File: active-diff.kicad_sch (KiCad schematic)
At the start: 13 parts, among them J1 INPUT+

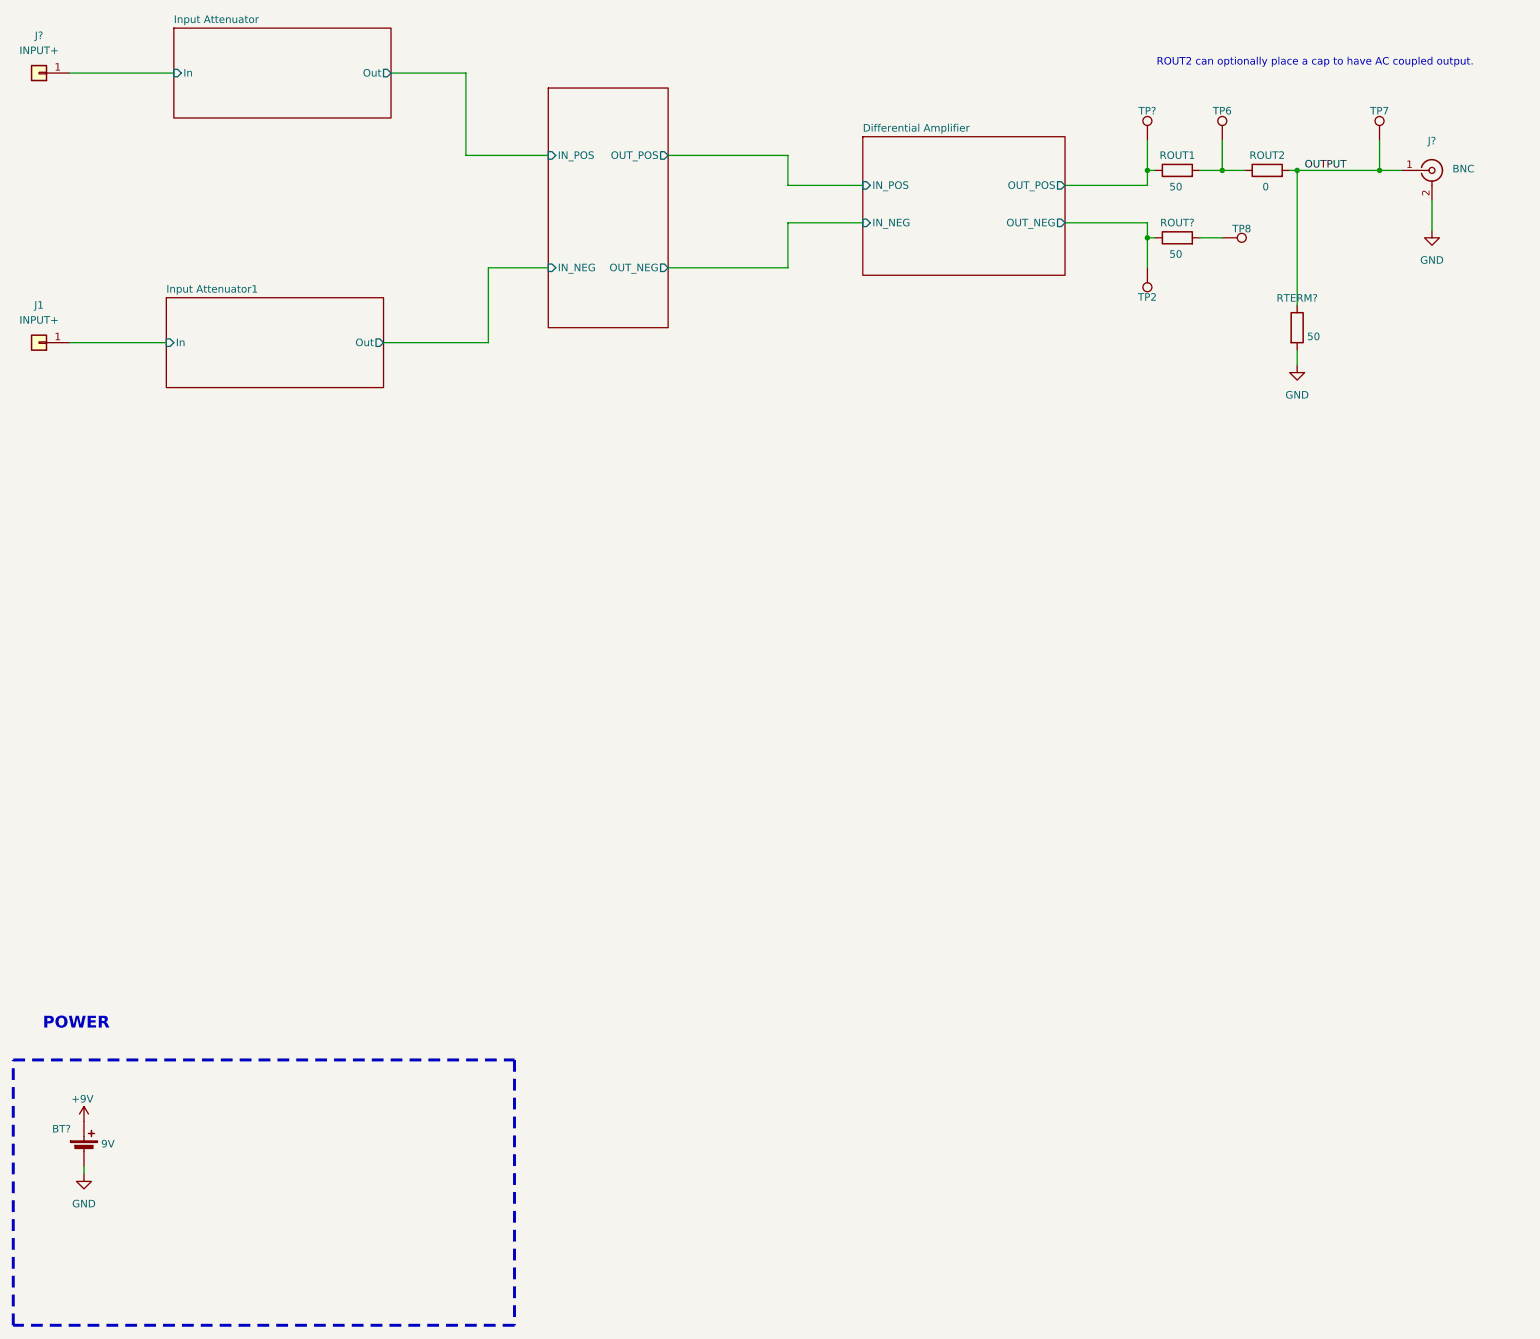
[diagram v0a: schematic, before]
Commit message: DRC completed. Need to add some 3D models.
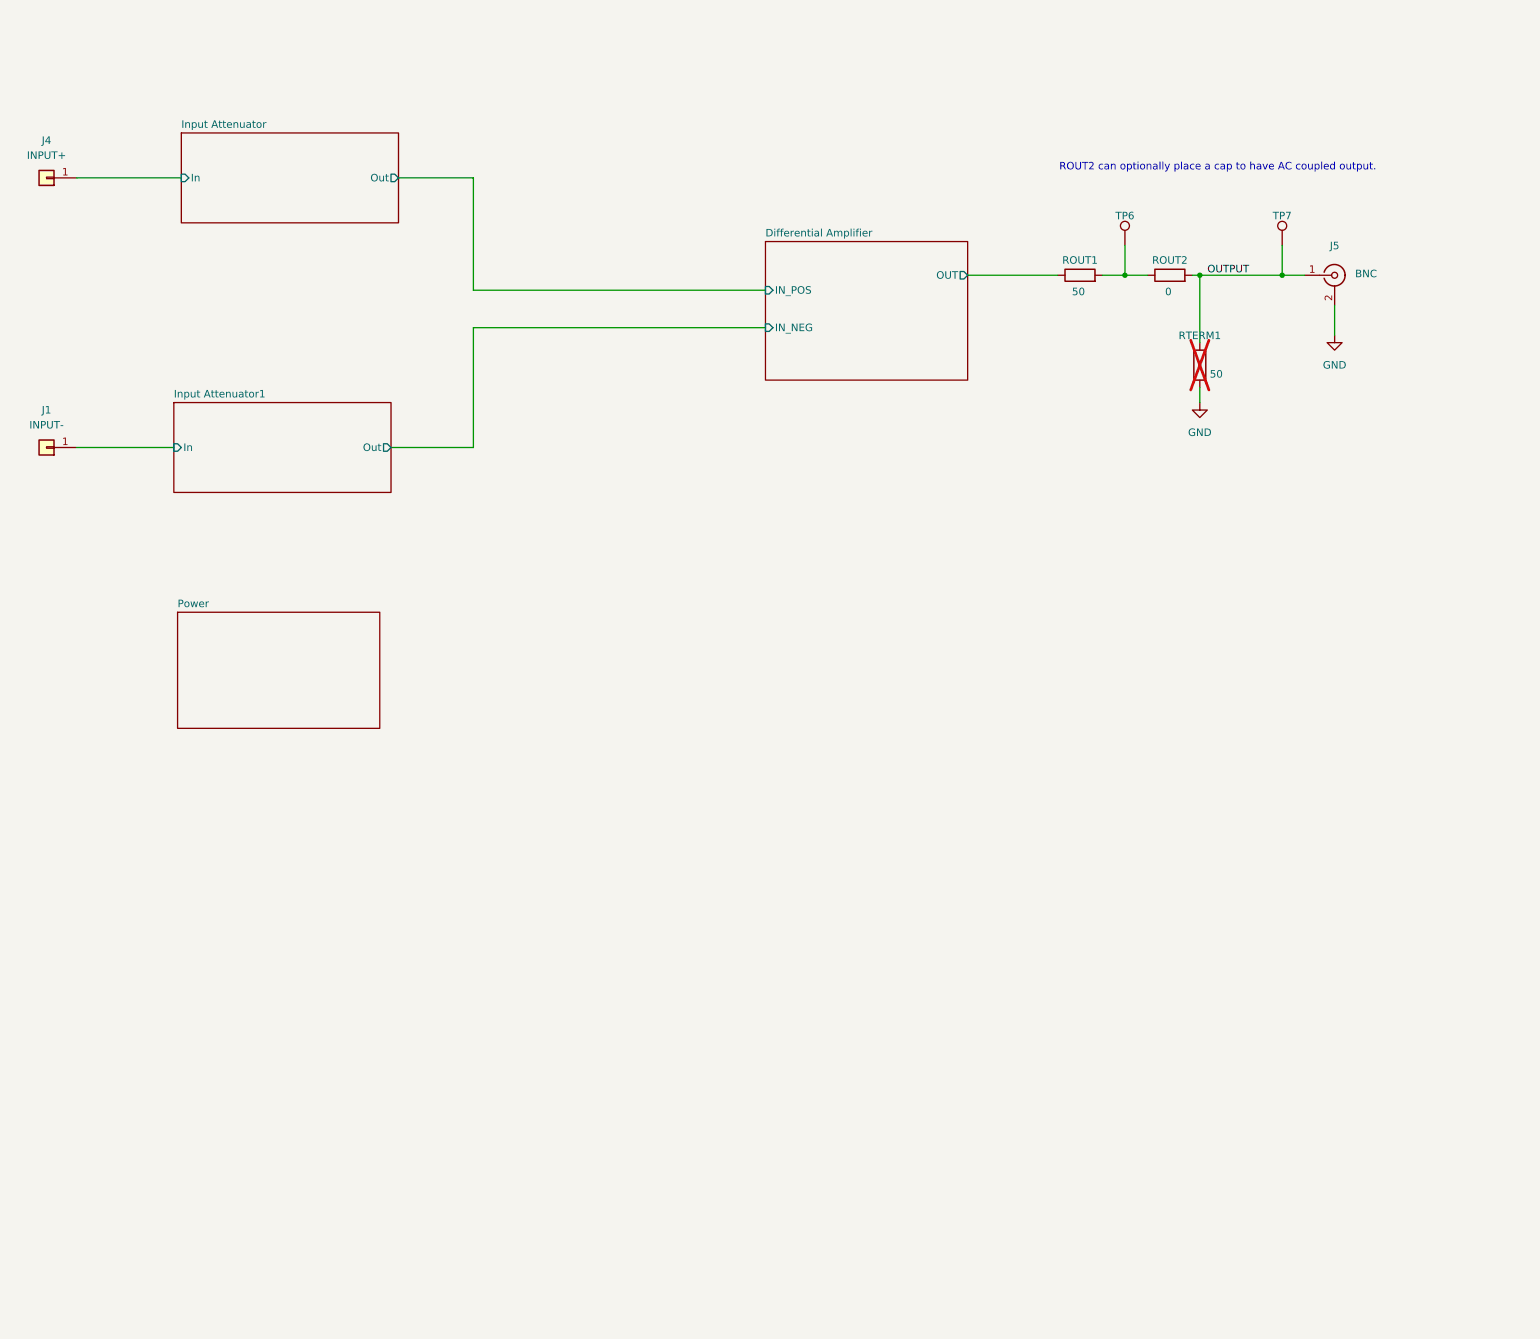
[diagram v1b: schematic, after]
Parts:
- removed BT?: 9V, Battery:BatteryHolder_Keystone_2460_1xAA, symbol Device:Battery_Cell
- removed ROUT?: 50, Resistor_SMD:R_0603_1608Metric, symbol Device:R
- removed TP2, TP8, TP?: TP, TestPoint:TestPoint_Pad_D2.0mm, symbol Connector:TestPoint
- J1: value INPUT+ -> INPUT-; footprint Connector_PinHeader_2.54mm:PinHeader_1x01_P2.54mm_Vertical -> TestPoint:TestPoint_Pad_2.5x2.5mm
- J4: renamed from J?; footprint Connector_PinHeader_2.54mm:PinHeader_1x01_P2.54mm_Vertical -> TestPoint:TestPoint_Pad_2.5x2.5mm
- ROUT1, ROUT2: footprint Resistor_SMD:R_0603_1608Metric -> Resistor_SMD:R_0402_1005Metric_Pad0.72x0.64mm_HandSolder
- RTERM1: renamed from RTERM?; footprint Resistor_SMD:R_0603_1608Metric -> Resistor_SMD:R_0402_1005Metric_Pad0.72x0.64mm_HandSolder; now not fitted
- TP6, TP7: footprint TestPoint:TestPoint_Pad_D2.0mm -> TestPoint:TestPoint_Pad_D1.0mm
- gave numbers to parts that had none: 1
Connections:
- net Differential Amplifier/OUT_POS renamed Differential Amplifier/OUT
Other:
- removed sheet Buffers
- added sheet Power (Power.kicad_sch)
- sheet Differential Amplifier ports: added OUT; removed OUT_NEG, OUT_POS
- note removed: "POWER"
- moved on the sheet: J1, J4, J5, ROUT1, ROUT2, TP6, TP7

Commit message: R1 sent to JLCPCB
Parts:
- J1, J4, TP6, TP7: now left out of the parts list
- ROUT1: JLCPCB# (none) -> C227387
- ROUT2: JLCPCB# (none) -> C17168
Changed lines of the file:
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@@
 		(unit 1)
 		(exclude_from_sim no)
-		(in_bom yes)
+		(in_bom no)
 		(on_board yes)
 		(dnp no)
@@
 			)
 		)
+		(property "JLCPCB#" ""
+			(at 36.83 60.96 0)
+			(effects
+				(font
+					(size 1.27 1.27)
+				)
+				(hide yes)
+			)
+		)
 		(pin "1"
 		)
@@
 		)
 		(property "Description" "Output BNC connector"
+			(at 255.27 77.47 0)
+			(effects
+				(font
+					(size 1.27 1.27)
+				)
+				(hide yes)
+			)
+		)
+		(property "JLCPCB#" ""
 			(at 255.27 77.47 0)
 			(effects
@@
 			)
 		)
+		(property "JLCPCB#" ""
+			(at 232.41 92.71 0)
+			(effects
+				(font
+					(size 1.27 1.27)
+				)
+				(hide yes)
+			)
+		)
 		(pin "2"
 		)
@@
 			)
 		)
+		(property "JLCPCB#" "C17168"
+			(at 227.33 77.47 90)
+			(effects
+				(font
+					(size 1.27 1.27)
+				)
+				(hide yes)
+			)
+		)
 		(pin "1"
 		)
@@
 		(unit 1)
 		(exclude_from_sim no)
-		(in_bom yes)
+		(in_bom no)
 		(on_board yes)
 		(dnp no)
@@
 			)
 		)
+		(property "JLCPCB#" ""
+			(at 219.71 72.39 0)
+			(effects
+				(font
+					(size 1.27 1.27)
+				)
+				(hide yes)
+			)
+		)
 		(pin "1"
 		)
@@
 		(property "Description" "Output termination"
 			(at 212.09 77.47 0)
+			(effects
+				(font
+					(size 1.27 1.27)
+				)
+				(hide yes)
+			)
+		)
+		(property "JLCPCB#" "C227387"
+			(at 212.09 77.47 90)
 			(effects
 				(font
@@
 		(unit 1)
 		(exclude_from_sim no)
-		(in_bom yes)
+		(in_bom no)
 		(on_board yes)
 		(dnp no)
@@
 			)
 		)
+		(property "JLCPCB#" ""
+			(at 36.83 106.68 0)
+			(effects
+				(font
+					(size 1.27 1.27)
+				)
+				(hide yes)
+			)
+		)
 		(pin "1"
 		)
@@
 		(unit 1)
 		(exclude_from_sim no)
-		(in_bom yes)
+		(in_bom no)
 		(on_board yes)
 		(dnp no)
@@
 			(at 246.38 72.39 0)
 			(effects
+				(font
+					(size 1.27 1.27)
+				)
+				(hide yes)
+			)
+		)
+		(property "JLCPCB#" ""
+			(at 246.38 72.39 0)
+			(effects
